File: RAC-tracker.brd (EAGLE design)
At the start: 25.4 x 50.8 mm, 26 parts, among them J1 U.FL, J2 U.FL, J5 CORTEX_JTAG_DEBUG_MINIMUM_SMD, U1 NRF9160-SICA-R, U2 SIM-ST-MFF2, U3 MCP73831, U4 SKY65723-81, U5 MIC5365-1.8YC5-TR

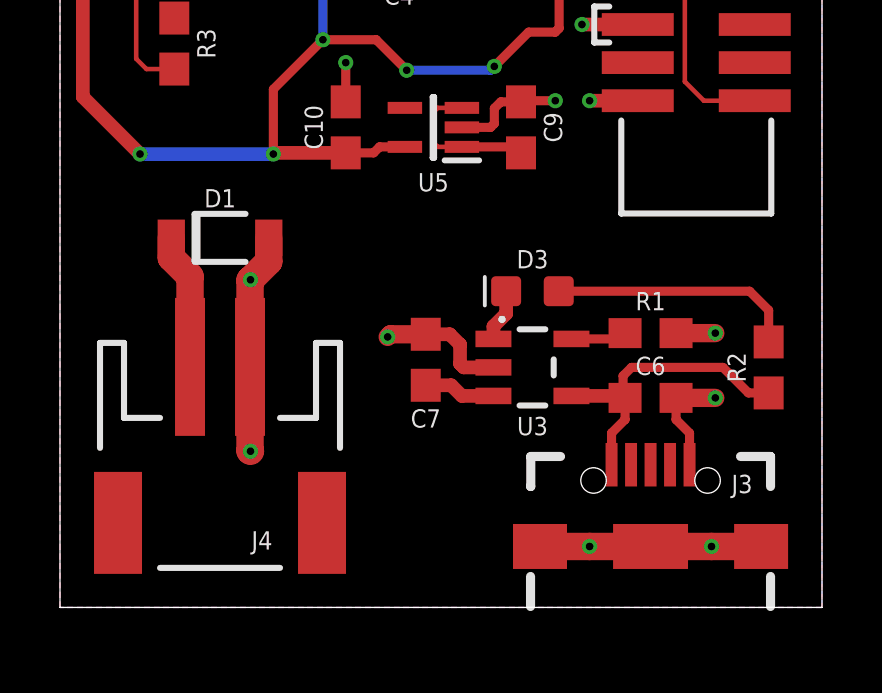
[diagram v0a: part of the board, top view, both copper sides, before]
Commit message: Added a purchasable Molex Micro-USB connector
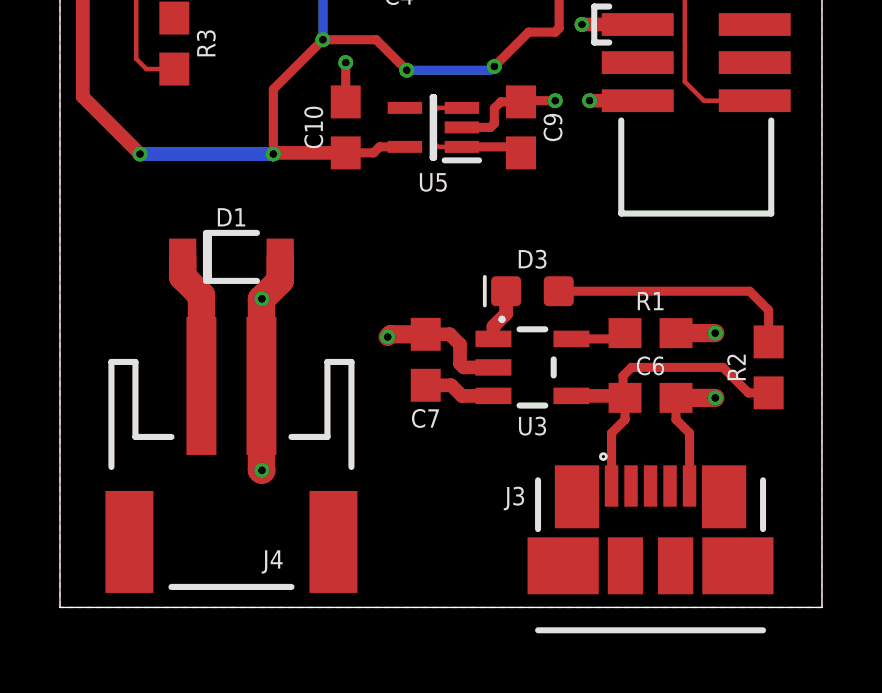
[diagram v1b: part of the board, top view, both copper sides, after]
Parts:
- J3: value (none) -> 47346-1001; device SparkFun-Connectors:USB-B-MICRO-SMD -> rocket-components:47346-0001
- moved J3 2.79 mm to (19.7, -0.76), turned to 180 degrees
- moved D1 0.74 mm to (5.71, 11.7)
- moved J4 0.74 mm to (5.71, 3.68)
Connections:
- removed net USB_DM: J3.D-
- removed net USB_DP: J3.D+
- net GND: now also J3.5; no longer J3.GND, J3.SHIELD1, J3.SHIELD2, J3.SHIELD3
- net V_USB: now also J3.1; no longer J3.VBUS
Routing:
- net GND: track 201.4 -> 194.8 mm, vias 124 -> 122
- net V_USB: track 10.2 -> 10.9 mm
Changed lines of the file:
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@@
 <attribute name="PROD_ID" value="CAP-00810" x="22.225" y="29.591" size="1.778" layer="27" rot="R270" display="off"/>
-</element>
-<element name="J3" library="SparkFun-Connectors" package="USB-B-MICRO-SMD" value="" x="19.685" y="2.032" smashed="yes" rot="R90">
-<attribute name="NAME" x="22.733" y="3.81" size="0.6096" layer="25" font="vector" ratio="20" align="bottom-center"/>
-<attribute name="PROD_ID" value="CONN-11752" x="19.685" y="2.032" size="1.778" layer="27" rot="R90" display="off"/>
-<attribute name="VALUE" x="24.384" y="0.762" size="0.6096" layer="27" font="vector" ratio="20" rot="R90" align="top-left"/>
 </element>
 <element name="U3" library="SparkFun-IC-Power" package="SOT23-5" value="MCP73831" x="15.748" y="8.001" smashed="yes" rot="R270">
@@
 <attribute name="PROD_ID" value="RES-07856" x="23.622" y="8.001" size="1.778" layer="27" rot="R270" display="off"/>
 </element>
-<element name="J4" library="SparkFun-Connectors" package="JST-2-SMD" value="" x="5.334" y="4.318" smashed="yes" rot="R180">
-<attribute name="NAME" x="6.731" y="2.54" size="0.6096" layer="25" font="vector" ratio="20" rot="R180" align="bottom-center"/>
-<attribute name="PROD_ID" value="CONN-11443" x="5.334" y="4.318" size="1.778" layer="27" rot="R180" display="off"/>
-<attribute name="SF_ID" value="PRT-08612" x="5.334" y="4.318" size="1.778" layer="27" rot="R180" display="off"/>
-<attribute name="VALUE" x="6.985" y="3.683" size="0.6096" layer="27" font="vector" ratio="20" rot="R180"/>
+<element name="J4" library="SparkFun-Connectors" package="JST-2-SMD" value="" x="5.715" y="3.683" smashed="yes" rot="R180">
+<attribute name="NAME" x="7.112" y="1.905" size="0.6096" layer="25" font="vector" ratio="20" rot="R180" align="bottom-center"/>
+<attribute name="PROD_ID" value="CONN-11443" x="5.715" y="3.683" size="1.778" layer="27" rot="R180" display="off"/>
+<attribute name="SF_ID" value="PRT-08612" x="5.715" y="3.683" size="1.778" layer="27" rot="R180" display="off"/>
+<attribute name="VALUE" x="7.366" y="3.048" size="0.6096" layer="27" font="vector" ratio="20" rot="R180"/>
 </element>
 <element name="U1" library="rocket-components" package="NORDIC_NRF9160-SICA-R" value="NRF9160-SICA-R" x="9.271" y="31.369" smashed="yes" rot="R90">
@@
 <attribute name="SF_ID" value="WRL-09144" x="2.921" y="47.625" size="1.778" layer="27" rot="R270" display="off"/>
 </element>
-<element name="D1" library="diode" library_urn="urn:adsk.eagle:library:210" package="SOD123FL" package3d_urn="urn:adsk.eagle:package:43458/1" value="SMF5.0AT1" x="5.334" y="12.319" smashed="yes">
-<attribute name="NAME" x="5.334" y="13.335" size="0.6096" layer="25" font="vector" ratio="20" align="bottom-center"/>
-<attribute name="POPULARITY" value="2" x="5.334" y="12.319" size="1.778" layer="27" display="off"/>
+<element name="D1" library="diode" library_urn="urn:adsk.eagle:library:210" package="SOD123FL" package3d_urn="urn:adsk.eagle:package:43458/1" value="SMF5.0AT1" x="5.715" y="11.684" smashed="yes">
+<attribute name="NAME" x="5.715" y="12.7" size="0.6096" layer="25" font="vector" ratio="20" align="bottom-center"/>
+<attribute name="POPULARITY" value="2" x="5.715" y="11.684" size="1.778" layer="27" display="off"/>
 </element>
 <element name="C4" library="rocket-components" package="CAPC2012X145N" value="47uF" x="11.303" y="21.717" smashed="yes">
@@
 <attribute name="PROD_ID" value="CONN-14503" x="21.209" y="19.431" size="1.778" layer="27" rot="R90" display="off"/>
 </element>
+<element name="J3" library="rocket-components" package="47346-0001" value="47346-1001" x="19.685" y="-0.762" smashed="yes" rot="R180">
+<attribute name="DESCRIPTION" value="MOLEX - 47346-1001 - MULTIPOLE CONNECTOR" x="19.685" y="-0.762" size="1.778" layer="27" rot="R180" display="off"/>
+<attribute name="HEIGHT" value="mm" x="19.685" y="-0.762" size="1.778" layer="27" rot="R180" display="off"/>
+<attribute name="MANUFACTURER_NAME" value="Molex" x="19.685" y="-0.762" size="1.778" layer="27" rot="R180" display="off"/>
+<attribute name="MANUFACTURER_PART_NUMBER" value="47346-1001" x="19.685" y="-0.762" size="1.778" layer="27" rot="R180" display="off"/>
+<attribute name="MOUSER_PART_NUMBER" value="538-47346-1001" x="19.685" y="-0.762" size="1.778" layer="27" rot="R180" display="off"/>
+<attribute name="MOUSER_PRICE-STOCK" value="https://www.mouser.com/Search/Refine.aspx?Keyword=538-47346-1001" x="19.685" y="-0.762" size="1.778" layer="27" rot="R180" display="off"/>
+<attribute name="NAME" x="15.181" y="3.405" size="0.6096" layer="25" font="vector" ratio="20" align="bottom-center"/>
+<attribute name="VALUE" x="19.998" y="2.818" size="1.27" layer="27" rot="R180" align="center"/>
+</element>
 </elements>
 <signals>
@@
 <contactref element="C5" pad="2"/>
 <contactref element="U2" pad="9"/>
-<contactref element="J3" pad="SHIELD1"/>
-<contactref element="J3" pad="SHIELD2"/>
-<contactref element="J3" pad="SHIELD3"/>
-<contactref element="J3" pad="GND"/>
 <contactref element="R1" pad="1"/>
 <contactref element="C7" pad="2"/>
@@
 <wire x1="20.535" y1="9.144" x2="21.844" y2="9.144" width="0.6096" layer="1"/>
 <via x="21.844" y="9.144" extent="1-16" drill="0.254"/>
-<wire x1="16" y1="2.032" x2="17.653" y2="2.032" width="0.9144" layer="1"/>
-<via x="17.653" y="2.032" extent="1-16" drill="0.254"/>
-<wire x1="23.37" y1="2.032" x2="21.717" y2="2.032" width="0.9144" layer="1"/>
-<via x="21.717" y="2.032" extent="1-16" drill="0.254"/>
-<wire x1="19.685" y1="2.032" x2="17.653" y2="2.032" width="0.9144" layer="1"/>
-<wire x1="19.685" y1="2.032" x2="21.717" y2="2.032" width="0.9144" layer="1"/>
-<wire x1="20.985" y1="4.757" x2="20.985" y2="5.812" width="0.3048" layer="1"/>
 <wire x1="20.535" y1="6.262" x2="20.535" y2="6.985" width="0.3048" layer="1"/>
 <wire x1="20.985" y1="5.812" x2="20.535" y2="6.262" width="0.3048" layer="1"/>
@@
 <via x="21.336" y="38.481" extent="1-16" drill="0.254"/>
 <wire x1="22.225" y1="38.1" x2="21.844" y2="38.481" width="0.4572" layer="1"/>
-<wire x1="6.334" y1="8.018" x2="6.334" y2="10.906" width="0.9144" layer="1"/>
-<wire x1="6.334" y1="10.906" x2="6.35" y2="10.922" width="0.9144" layer="1"/>
-<via x="6.35" y="10.922" extent="1-16" drill="0.254"/>
-<wire x1="6.959" y1="12.319" x2="6.959" y2="11.531" width="0.9144" layer="1"/>
-<wire x1="6.959" y1="11.531" x2="6.35" y2="10.922" width="0.9144" layer="1"/>
-<wire x1="6.334" y1="8.018" x2="6.334" y2="5.223" width="0.9144" layer="1"/>
-<wire x1="6.334" y1="5.223" x2="6.35" y2="5.207" width="0.9144" layer="1"/>
-<via x="6.35" y="5.207" extent="1-16" drill="0.254"/>
+<wire x1="6.715" y1="7.383" x2="6.715" y2="10.271" width="0.9144" layer="1"/>
+<wire x1="6.715" y1="10.271" x2="6.731" y2="10.287" width="0.9144" layer="1"/>
+<via x="6.731" y="10.287" extent="1-16" drill="0.254"/>
+<wire x1="7.34" y1="11.684" x2="7.34" y2="10.896" width="0.9144" layer="1"/>
+<wire x1="7.34" y1="10.896" x2="6.731" y2="10.287" width="0.9144" layer="1"/>
+<wire x1="6.715" y1="7.383" x2="6.715" y2="4.588" width="0.9144" layer="1"/>
+<wire x1="6.715" y1="4.588" x2="6.731" y2="4.572" width="0.9144" layer="1"/>
+<via x="6.731" y="4.572" extent="1-16" drill="0.254"/>
 <wire x1="22.225" y1="37.221" x2="22.225" y2="36.576" width="0.4572" layer="1"/>
 <wire x1="22.225" y1="36.576" x2="20.32" y2="34.671" width="0.4572" layer="1"/>
@@
 <via x="22.4663" y="47.664" extent="1-16" drill="0.254"/>
 <via x="6.35" y="45.593" extent="1-16" drill="0.254"/>
+<contactref element="J3" pad="5"/>
+<wire x1="20.985" y1="4.048" x2="20.985" y2="5.812" width="0.3048" layer="1"/>
 </signal>
 <signal name="SIM_VIN">
@@
 <wire x1="13.042" y1="7.405" x2="12.192" y2="7.405" width="0.4572" layer="1"/>
 <wire x1="13.396" y1="7.051" x2="13.042" y2="7.405" width="0.4572" layer="1"/>
-<wire x1="3.709" y1="12.319" x2="3.709" y2="11.658" width="0.9144" layer="1"/>
-<wire x1="4.334" y1="11.033" x2="4.334" y2="8.018" width="0.9144" layer="1"/>
-<wire x1="3.709" y1="11.658" x2="4.334" y2="11.033" width="0.9144" layer="1"/>
+<wire x1="4.09" y1="11.684" x2="4.09" y2="11.023" width="0.9144" layer="1"/>
+<wire x1="4.715" y1="10.398" x2="4.715" y2="7.383" width="0.9144" layer="1"/>
+<wire x1="4.09" y1="11.023" x2="4.715" y2="10.398" width="0.9144" layer="1"/>
 <wire x1="3.849" y1="21.844" x2="3.849" y2="22.694" width="0.3048" layer="1"/>
 <wire x1="3.429" y1="23.114" x2="3.429" y2="23.876" width="0.3048" layer="1"/>
@@
 </signal>
 <signal name="V_USB">
-<contactref element="J3" pad="VBUS"/>
 <contactref element="R2" pad="2"/>
 <contactref element="U3" pad="4"/>
 <contactref element="C6" pad="1"/>
-<wire x1="18.385" y1="4.757" x2="18.385" y2="5.812" width="0.3048" layer="1"/>
 <wire x1="18.835" y1="6.262" x2="18.835" y2="6.985" width="0.3048" layer="1"/>
 <wire x1="18.385" y1="5.812" x2="18.835" y2="6.262" width="0.3048" layer="1"/>
@@
 <wire x1="22.098" y1="8.001" x2="19.05" y2="8.001" width="0.3048" layer="1"/>
 <wire x1="19.05" y1="8.001" x2="18.769" y2="7.72" width="0.3048" layer="1"/>
-</signal>
-<signal name="USB_DM">
-<contactref element="J3" pad="D-"/>
-</signal>
-<signal name="USB_DP">
-<contactref element="J3" pad="D+"/>
+<contactref element="J3" pad="1"/>
+<wire x1="18.385" y1="4.048" x2="18.385" y2="5.812" width="0.3048" layer="1"/>
 </signal>
 <signal name="PROG">

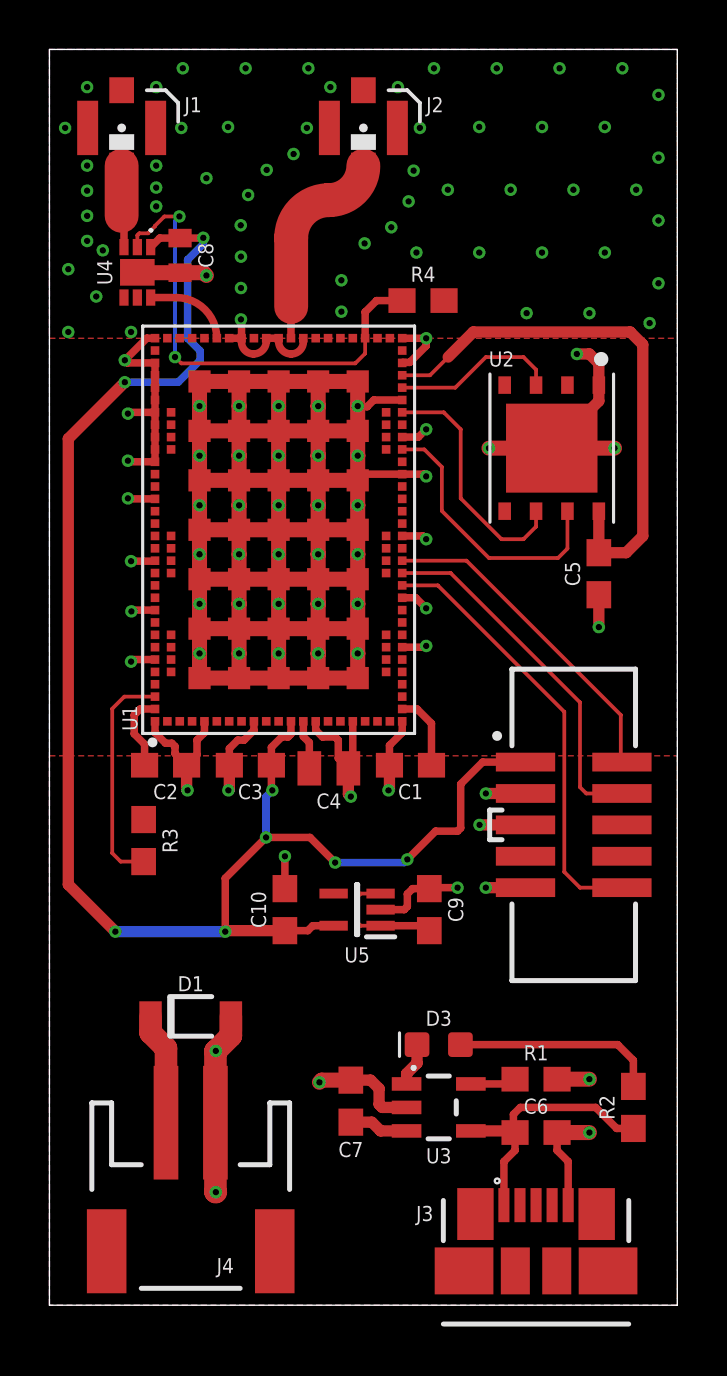
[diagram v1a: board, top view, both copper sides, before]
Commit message: U.FL replaced to fit BOM, polygons adjusted. Fab ready!
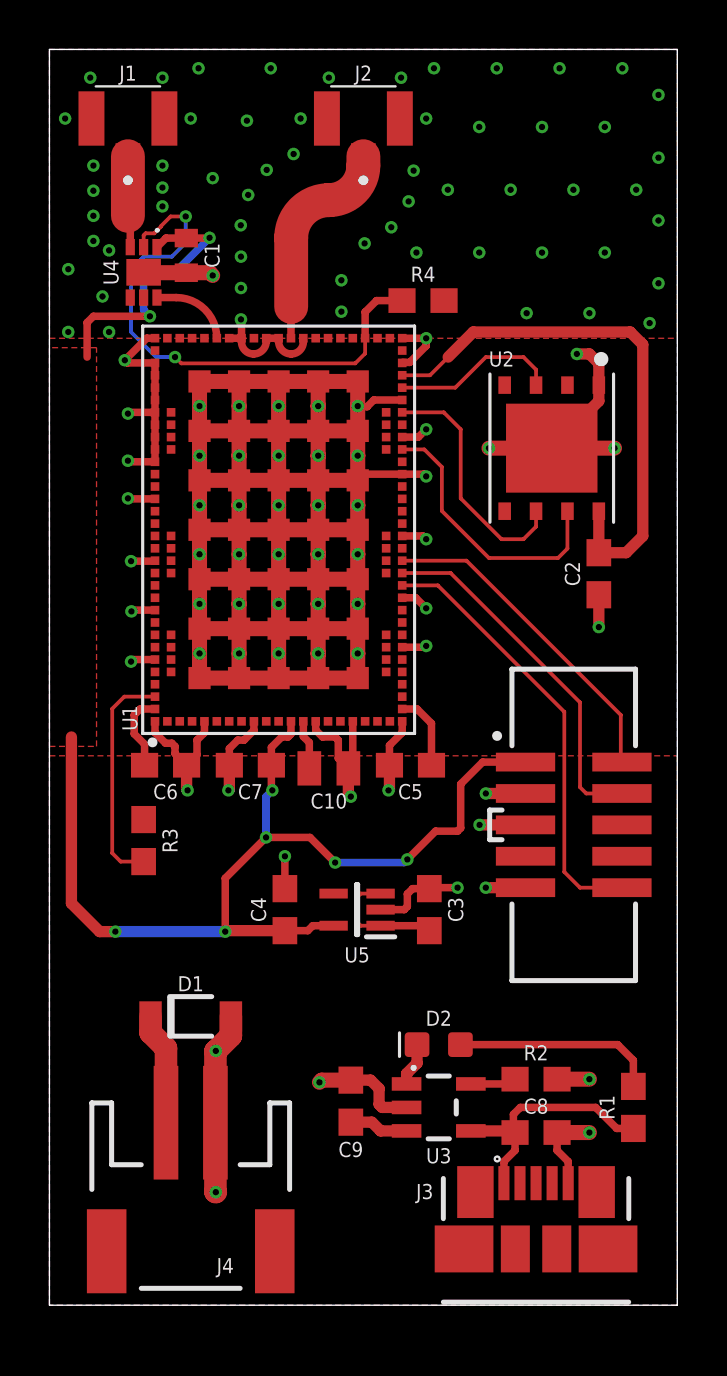
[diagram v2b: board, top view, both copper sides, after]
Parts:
- C1: value 4.7uF -> 56pF; device SparkFun-Capacitors:0603 -> rocket-components:CAPC1608X90N
- C10: value 1.0uF -> 47uF; device SparkFun-Capacitors:0603 -> rocket-components:CAPC2012X145N
- C2: value 4.7uF -> 0.1uF
- C3: value 4.7uF -> 1.0uF
- C4: value 47uF -> 1.0uF; device rocket-components:CAPC2012X145N -> SparkFun-Capacitors:0603
- C5: value 0.1uF -> 4.7uF
- C8: value 56pF -> 4.7uF; device rocket-components:CAPC1608X90N -> SparkFun-Capacitors:0603
- C9: value 1.0uF -> 4.7uF
- J1, J2: value U.FL -> 2337019-1; device SparkFun-Connectors:U.FL -> rocket-components:23370191
- R1: value 2.0k -> 1k
- R2: value 1k -> 2.0k
- moved C8 38.3 mm to (19.7, 6.99), turned to 0 degrees
- moved C1 22.5 mm to (5.54, 42.5), turned to 270 degrees
- moved C6 21.1 mm to (4.70, 21.8)
- moved C2 19.2 mm to (22.2, 29.6), turned to 270 degrees
- moved C7 14.2 mm to (8.13, 21.8), turned to 180 degrees
- moved C5 10.9 mm to (14.6, 21.8), turned to 180 degrees
- moved C3 9.30 mm to (15.4, 16.0), turned to 90 degrees
- moved C9 8.37 mm to (12.2, 8.26)
- moved C10 5.99 mm to (11.3, 21.7), turned to 0 degrees
- moved C4 5.99 mm to (9.53, 16.0), turned to 90 degrees
- moved R1 4.10 mm to (23.6, 8.00), turned to 270 degrees
- moved R2 4.10 mm to (19.7, 9.14), turned to 180 degrees
- moved J3 0.89 mm to (19.7, 0.13)
- moved J1 0.46 mm to (3.17, 48.0), turned to 0 degrees
- moved J2 0.38 mm to (12.7, 48.0), turned to 0 degrees
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- renumbered D3 to D2
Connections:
- net 1.8V: now also C1.1, C4.1, C7.1; no longer C10.1, C3.1, C8.1
- net GND: now also J1.3, J2.3, R2.1; no longer J1.1, J2.1, R1.1
- net GPS_ANT: now also J1.1; no longer J1.FEED
- net IO_SUP: now also C10.1; no longer C4.1
- net LTE_ANT: now also J2.1; no longer J2.FEED
- net PROG: now also R2.2; no longer R1.2
- net SIM_VIN: now also C2.1; no longer C5.1
- net STAT_AN: now also R1.1; no longer R2.1
- net V_BATT: now also C3.1, C5.1, C6.1; no longer C1.1, C2.1, C7.1
- net V_USB: now also C8.1, R1.2; no longer C6.1, R2.2
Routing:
- net 1.8V: track 67.4 -> 52.7 mm
- net GPS_EN: track 19.6 -> 22.3 mm
- net GND: track 194.8 -> 193.9 mm, vias 122 -> 121
- net V_USB: track 10.9 -> 10.0 mm
- added copper zone on layer 1, net 1.8V
